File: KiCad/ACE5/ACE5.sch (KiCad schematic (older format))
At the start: 75 parts, among them Q3 BC183, U1 LM7805_TO220, X2 5MHz

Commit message: re order pcbs and some logic. Move transistor
Signed-off-by: John Bradley <flypie@rocketmail.com>
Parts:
- removed AUDIO-IN1, AUDIO-OUT1: Conn_01x02, Connector_PinHeader_2.54mm:PinHeader_1x02_P2.54mm_Vertical, symbol Connector_Generic:Conn_01x02
- removed C3: 47nF, Capacitor_THT:C_Disc_D3.0mm_W1.6mm_P2.50mm, symbol Device:C
- removed C5, C6: 47nF, Capacitor_THT:C_Disc_D3.0mm_W1.6mm_P2.50mm, symbol Device:C_Small
- removed D1, D2, D3, D4, D5, D6, D7, D8, D9: 1N4148, Diode_THT:D_DO-35_SOD27_P2.54mm_Vertical_AnodeUp, symbol Diode:1N4148
- removed KEYBOARD1: Conn_02x08_Odd_Even, Connector_PinHeader_2.54mm:PinHeader_2x08_P2.54mm_Vertical, symbol Connector_Generic:Conn_02x08_Odd_Even
- removed Q3: BC183, Package_TO_SOT_THT:TO-92_Inline, symbol Device:Q_NPN_CBE
- removed R10: 10k, Resistor_THT:R_Axial_DIN0204_L3.6mm_D1.6mm_P2.54mm_Vertical, symbol Device:R
- removed R110: 200, Resistor_THT:R_Axial_DIN0204_L3.6mm_D1.6mm_P2.54mm_Vertical, symbol Device:R
- removed R5: 12k, Resistor_THT:R_Axial_DIN0204_L3.6mm_D1.6mm_P2.54mm_Vertical, symbol Device:R
- removed R6: 1K, Resistor_THT:R_Axial_DIN0204_L3.6mm_D1.6mm_P2.54mm_Vertical, symbol Device:R
- removed R9: 22k, Resistor_THT:R_Axial_DIN0204_L3.6mm_D1.6mm_P2.54mm_Vertical, symbol Device:R
- removed SPK1: SPK1, Connector_PinHeader_2.54mm:PinHeader_1x02_P2.54mm_Vertical, symbol Connector_Generic:Conn_01x02
- removed unit 2 of Z102
- removed Z103: 74AHCT02, Package_DIP:DIP-14_W7.62mm, symbol 74xx:74HCT02
- removed Z14, Z15: 74AHCT367, Package_DIP:DIP-16_W7.62mm, symbol 74xx:74LS367
- removed unit 2 of Z24
- removed unit 3 of Z24
- removed unit 4 of Z24
- removed unit 1 of Z24
- removed unit 1 of Z27
- added Logo1: ZilogFront, Symbol:ZilogInsideFront, symbol Graphic:ZilogFront
- added Logo2: ZilogBack, Symbol:ZilogInsideBack, symbol Graphic:ZilogBack
- C10, C100, C101, C13, C14, C15, C16, C17, C18, C19, C20, C21: footprint Capacitor_THT:C_Disc_D3.0mm_W1.6mm_P2.50mm -> Capacitor_THT:C_Disc_D4.3mm_W1.9mm_P5.00mm
- X2: value 5MHz -> 32MHz
- Z102: value 74AHCT04 -> SN74AHCT04N
- Z104: footprint Package_DIP:DIP-14_W7.62mm -> Package_SO:SOIC-14_3.9x8.7mm_P1.27mm
- Z104: footprint (none) -> Package_SO:SOIC-14_3.9x8.7mm_P1.27mm
- Z24: value 74AHCT02 -> SN74AHCT02N
- Z27: value 74AHCT74 -> SN74AHCT74N
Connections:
- net labels added: PHI, ~TAPECS
- net labels removed: IOREQ&11111110B, ~CPUCLK
- wire segments 509 -> 396
- no-connect marks 61 -> 35
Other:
- moved on the sheet: C10, C100, C101, C11, C12, C13, C14, C15, C16, C17, C18, C19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

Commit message: Update to Version of ACE3 sent off and update subsequent models to near that level.
Signed-off-by: John Bradley <flypie@rocketmail.com>
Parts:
- removed Z108: 74AHCT08, Package_DIP:DIP-14_W7.62mm, symbol 74xx:74LS08
- Z1-2: value 27256 -> SST39SF010-LCC; symbol Memory_EPROM:27C512PLCC -> Memory_Flash:SST39SF010-LCC
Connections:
- wire segments 396 -> 392
- no-connect marks 35 -> 30
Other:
- moved on the sheet: Z100A, Z101B, Z102E, Z102F, Z19C, Z19D, Z23A, Z23B, Z25C

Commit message: Update Post ACE4 Boards. Add MPU to eZ80 for Keyboard. Add eZ80 RAM card. Split MMU and PSU into own sub-schema.
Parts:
- removed C10, C13, C14, C15, C16, C17, C18, C19, C20, C21: 100nf, Capacitor_THT:C_Disc_D4.3mm_W1.9mm_P5.00mm, symbol Device:C
- removed C11: 100uf, Capacitor_THT:CP_Radial_D4.0mm_P1.50mm, symbol Device:CP
- removed C12: 100uf, Capacitor_THT:CP_Radial_D5.0mm_P2.00mm, symbol Device:CP
- removed C9: 100u, Capacitor_THT:CP_Radial_D5.0mm_P2.00mm, symbol Device:CP
- removed L1: 100 nH, Inductor_THT:L_Axial_L13.0mm_D4.5mm_P5.08mm_Vertical_Fastron_HCCC, symbol Device:L
- removed POWER-9V-DC1: PJ-036C, cuipj:CUI_PJ-036C, symbol PJ-036C:PJ-036C
- removed U1: LM7805_TO220, Package_TO_SOT_THT:TO-220-3_Vertical, symbol Regulator_Linear:LM7805_TO220
- removed Z10, Z11, Z9: 74AHCT393, Package_DIP:DIP-14_W7.62mm, symbol 74xx:74LS393
- removed unit 3 of Z100
- removed unit 2 of Z101
- removed unit 3 of Z101
- removed unit 7 of Z102
- removed unit 2 of Z104
- removed Z105, Z106: 74AHCT365, Package_DIP:DIP-16_W7.62mm, symbol 74xx:74LS365
- removed Z107: 74AHCT273, Package_DIP:DIP-20_W7.62mm, symbol 74xx:74LS273
- removed unit 5 of Z19
- removed Z20: 74AHCT08, Package_DIP:DIP-14_W7.62mm, symbol 74xx:74LS08
- removed Z21: 74AHCT11, Package_DIP:DIP-14_W7.62mm, symbol 74xx:74LS11
- removed unit 4 of Z22
- removed unit 5 of Z23
- removed Z24: SN74AHCT02N, Package_DIP:DIP-14_W7.62mm, symbol 74xx:74HCT02
- removed unit 5 of Z25
- removed Z27: SN74AHCT74N, Package_DIP:DIP-14_W7.62mm, symbol 74xx:74LS74
- Z101: renamed from Z104; value 74AHCT30 -> 74AHCT30D
- Z104: renamed from Z101; value 74AHCT21 -> 74AHCT30D; footprint Package_DIP:DIP-14_W7.62mm -> Package_SO:SOIC-14_3.9x8.7mm_P1.27mm; symbol 74xx:74LS21 -> 74xx:74LS30
- Z3-4: value AS6C4008-55PCN -> CY62158; footprint Package_SO:SOJ-36_10.16x23.49mm_P1.27mm -> Package_SO:TSOP-II-44_10.16x18.41mm_P0.8mm; symbol Memory_RAM:IS61C5128AL-10KLI -> SamacSys_Parts:CY62158-TSOP-II-44-PIN
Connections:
- net labels added: MA12, MA19, PAGED8K, ~PAGING
- net labels removed: +9V
- wire segments 392 -> 236
- no-connect marks 30 -> 27
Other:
- moved on the sheet: C100, C101, C7, R25, R32, X2, Z0B, Z1-2, Z100A, Z100B, Z101A, Z102B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

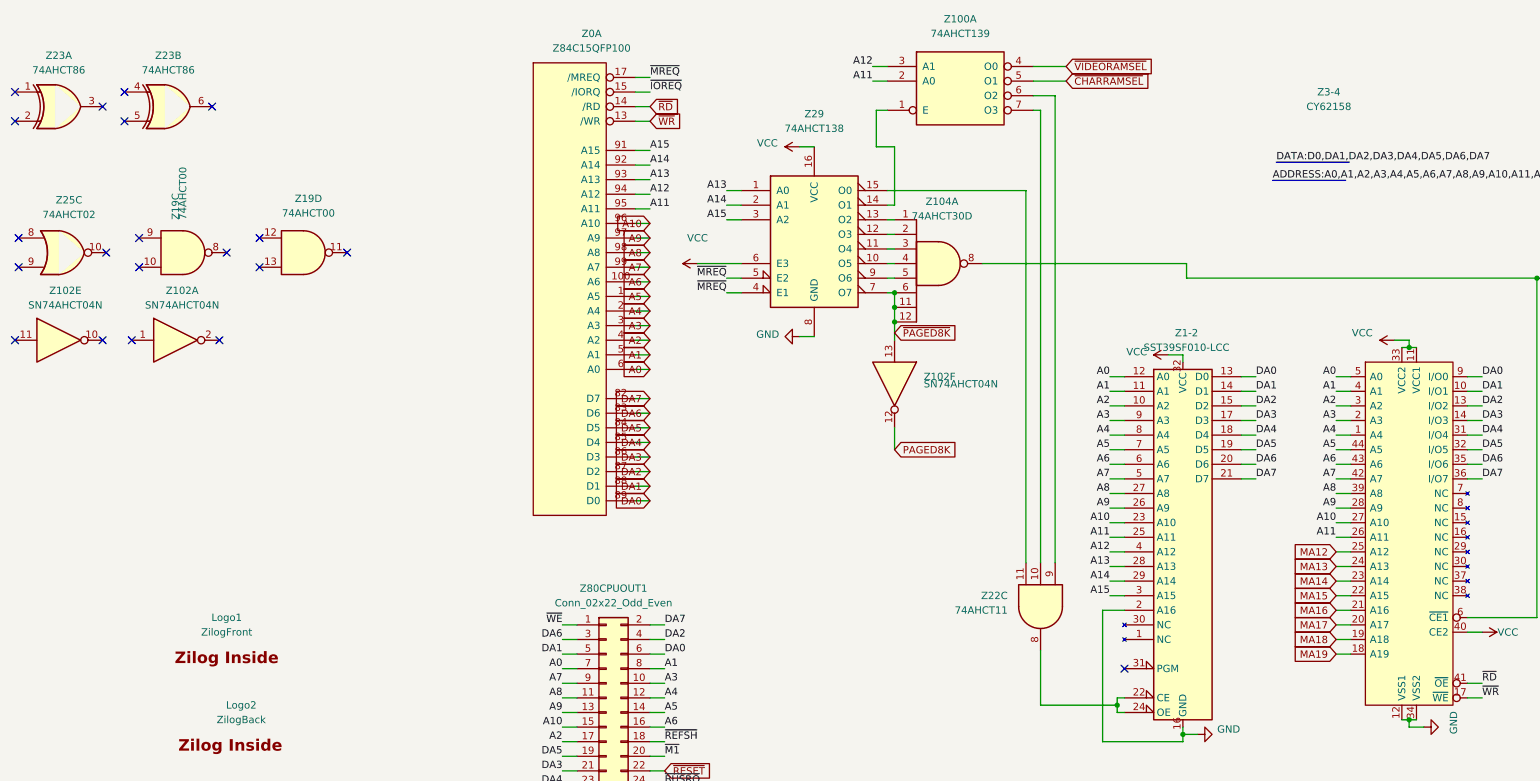
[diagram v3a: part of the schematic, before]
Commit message: Add example to UniBoard. Correct power and bus routing on ACEeZ80.jpg
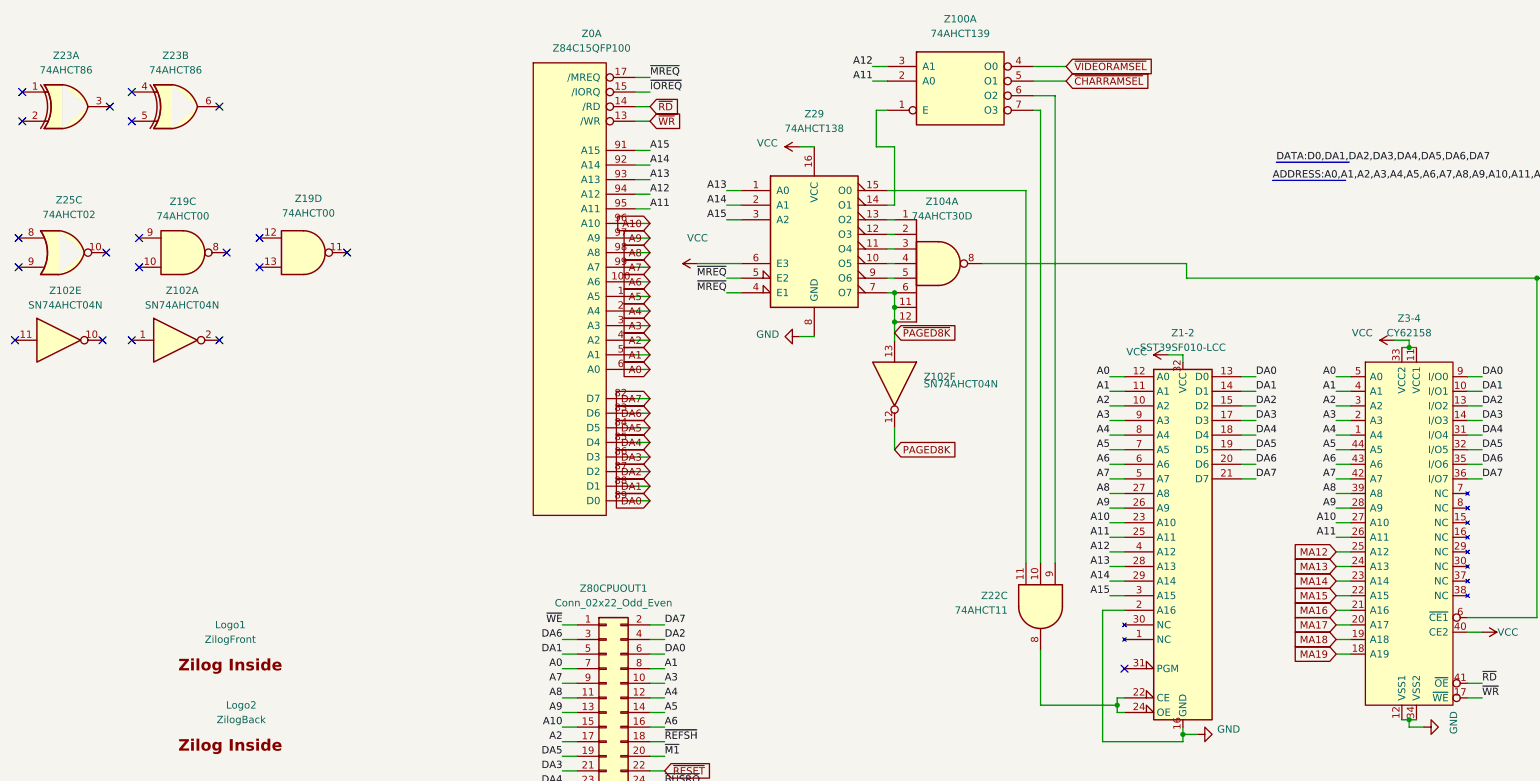
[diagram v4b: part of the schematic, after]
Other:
- moved on the sheet: Logo1, Z23A, Z23B
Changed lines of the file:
@@
 Text Label 8150 2275 0    50   ~ 0
 ~WE
-NoConn ~ -1900 1000
-NoConn ~ -1900 1200
-NoConn ~ -1300 1100
-NoConn ~ -2050 1100
-NoConn ~ -2650 1200
-NoConn ~ -2650 1000
+NoConn ~ -1850 1000
+NoConn ~ -1850 1200
+NoConn ~ -1250 1100
+NoConn ~ -2000 1100
+NoConn ~ -2600 1200
+NoConn ~ -2600 1000
 NoConn ~ 5425 6550
 $Sheet
@@
 U 1 1 5F80C898
 P 5050 2850
-F 0 "Z1-2" H 5375 3050 50  0000 C CNN
-F 1 "SST39SF010-LCC" H 5375 2950 50  0000 C CNN
+F 0 "Z1-2" H 5350 3050 50  0000 C CNN
+F 1 "SST39SF010-LCC" H 5350 2950 50  0000 C CNN
 F 2 "Package_LCC:PLCC-32_THT_Socket_11.4x14.0mm_P1.27mm" H 5050 2850 50  0001 C CNN
 F 3 "http:~/datasheet.octopart.com/D27256-2-Intel-datasheet-17852618.pdf" H 5050 2850 50  0001 C CNN
@@
 U 3 1 60726E0C
 P -1500 2100
-F 0 "Z19" V -1550 2325 50  0000 L CNN
-F 1 "74AHCT00" V -1500 2325 50  0000 L CNN
+F 0 "Z19" H -1500 2450 50  0000 C CNN
+F 1 "74AHCT00" H -1500 2350 50  0000 C CNN
 F 2 "Package_DIP:DIP-14_W7.62mm" H -1500 2100 50  0001 C CNN
 F 3 "http:~/www.ti.com/lit/gpn/sn74ls00" H -1500 2100 50  0001 C CNN
@@
 L 74xx:74LS86 Z23
 U 1 1 6061F7ED
-P -2350 1100
-F 0 "Z23" H -2350 1450 50  0000 C CNN
-F 1 "74AHCT86" H -2350 1350 50  0000 C CNN
-F 2 "Package_DIP:DIP-14_W7.62mm" H -2350 1100 50  0001 C CNN
-F 3 "74xx~74ls86.pdf" H -2350 1100 50  0001 C CNN
-	1    -2350 1100
+P -2300 1100
+F 0 "Z23" H -2300 1450 50  0000 C CNN
+F 1 "74AHCT86" H -2300 1350 50  0000 C CNN
+F 2 "Package_DIP:DIP-14_W7.62mm" H -2300 1100 50  0001 C CNN
+F 3 "74xx~74ls86.pdf" H -2300 1100 50  0001 C CNN
+	1    -2300 1100
 	1    0    0    -1
 $EndComp
@@
 L 74xx:74LS86 Z23
 U 2 1 60628B03
-P -1600 1100
-F 0 "Z23" H -1600 1450 50  0000 C CNN
-F 1 "74AHCT86" H -1600 1350 50  0000 C CNN
-F 2 "Package_DIP:DIP-14_W7.62mm" H -1600 1100 50  0001 C CNN
-F 3 "74xx~74ls86.pdf" H -1600 1100 50  0001 C CNN
-	2    -1600 1100
+P -1550 1100
+F 0 "Z23" H -1550 1450 50  0000 C CNN
+F 1 "74AHCT86" H -1550 1350 50  0000 C CNN
+F 2 "Package_DIP:DIP-14_W7.62mm" H -1550 1100 50  0001 C CNN
+F 3 "74xx~74ls86.pdf" H -1550 1100 50  0001 C CNN
+	2    -1550 1100
 	1    0    0    -1
 $EndComp
@@
 L Graphic:ZilogFront Logo1
 U 1 1 5E7922FA
-P -1550 4825
-F 0 "Logo1" H -1200 5050 50  0000 C CNN
-F 1 "ZilogFront" H -1200 4950 50  0000 C CNN
-F 2 "Symbol:ZilogInsideFront" H -1100 5075 50  0001 C CNN
-F 3 "" H -1550 4725 50  0001 C CNN
-	1    -1550 4825
+P -1525 4875
+F 0 "Logo1" H -1175 5100 50  0000 C CNN
+F 1 "ZilogFront" H -1175 5000 50  0000 C CNN
+F 2 "Symbol:ZilogInsideFront" H -1075 5125 50  0001 C CNN
+F 3 "" H -1525 4775 50  0001 C CNN
+	1    -1525 4875
 	1    0    0    -1
 $EndComp
@@
 U 1 1 5F80C976
 P 6600 2850
-F 0 "Z3-4" H 6350 4700 50  0000 C CNN
-F 1 "CY62158" H 6350 4600 50  0000 C CNN
+F 0 "Z3-4" H 6900 3150 50  0000 C CNN
+F 1 "CY62158" H 6900 3050 50  0000 C CNN
 F 2 "Package_SO:TSOP-II-44_10.16x18.41mm_P0.8mm" H 6600 2950 50  0001 C CNN
 F 3 "https:~/www.alliancememory.com/wp-content/uploads/pdf/AS6C4008.pdf" H 6600 2950 50  0001 C CNN
